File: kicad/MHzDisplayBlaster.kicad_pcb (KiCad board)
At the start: 2 copper layers, 50 x 39 mm, 10 parts, among them J1 Conn_02x15 DigitLHS, J2 Conn_02x15 DigitRHS, J3 Conn_01x03_Pin, J4 Conn_01x02_Pin, Q1 2N7000, U1 DC56-11GWA, U2 74HC04

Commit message: Add version silkscreen
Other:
- board text added: "V1.1"
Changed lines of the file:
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@@
+		)
+	)
+	(gr_text "V1.1"
+		(at 146.05 41.313236 0)
+		(layer "B.SilkS")
+		(effects
+			(font
+				(size 0.8 0.8)
+				(thickness 0.15)
+			)
+			(justify mirror)
 		)
 	)

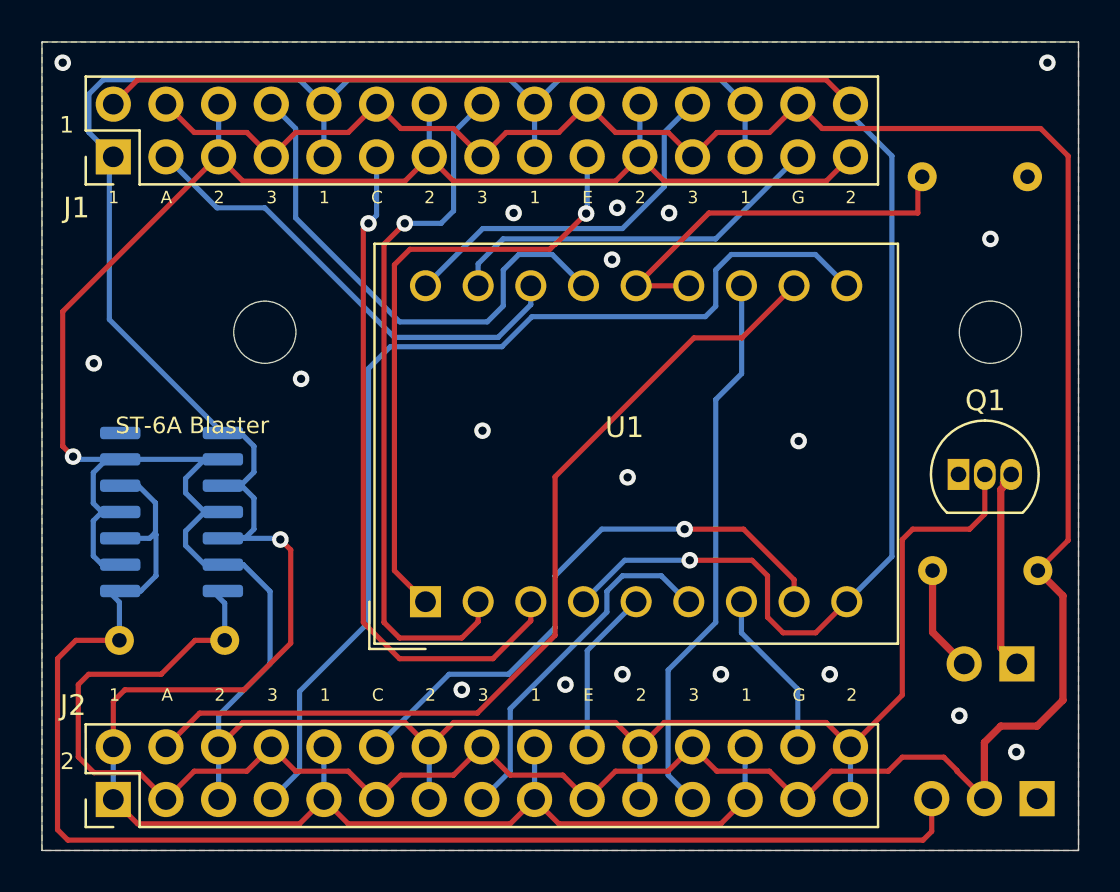
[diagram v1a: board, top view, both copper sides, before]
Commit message: v1.2 - surface mount and better power management
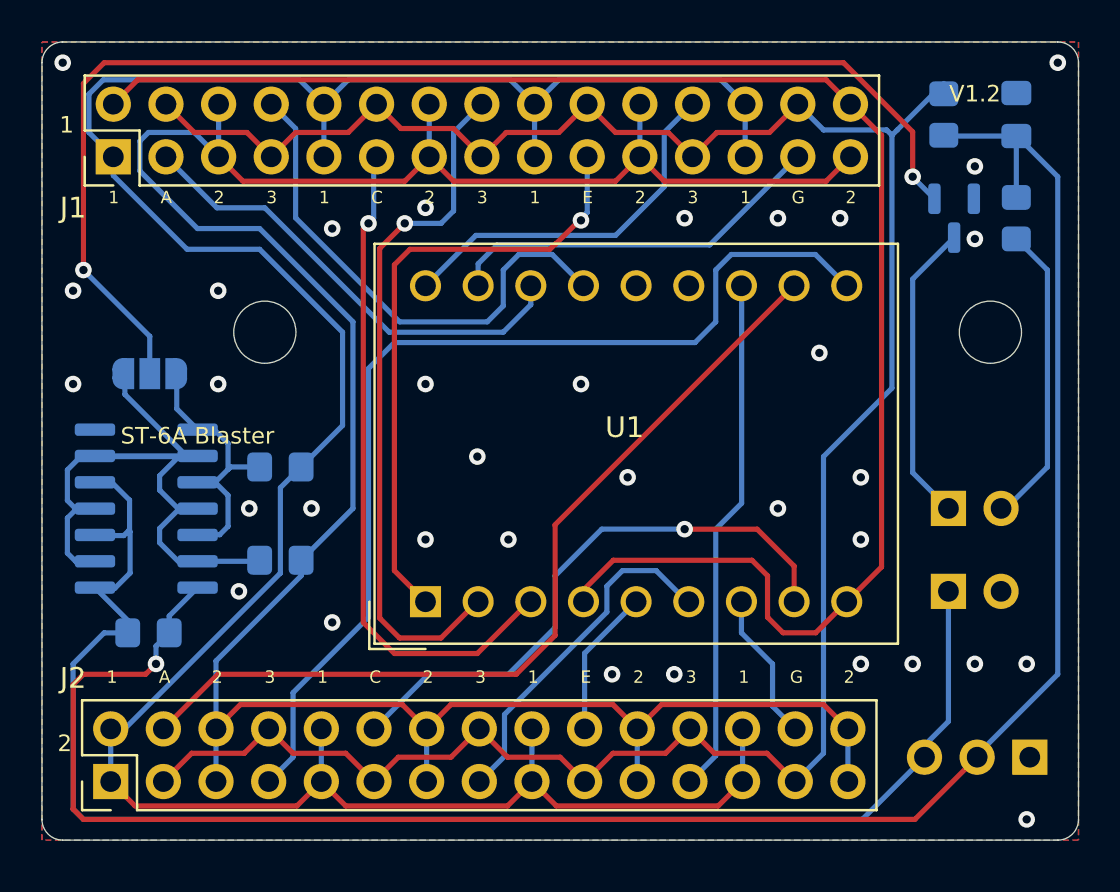
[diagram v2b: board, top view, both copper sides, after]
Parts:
- added C1: 10uf, Capacitor_SMD:C_0805_2012Metric_Pad1.18x1.45mm_HandSolder, B.Cu at (147.0, 43.5)
- added J5: SW, Connector_PinHeader_2.54mm:PinHeader_1x02_P2.54mm_Vertical, B.Cu at (143.7, 66.5)
- added JP1: Jumper_3_Open, Jumper:SolderJumper-3_P1.3mm_Open_RoundedPad1.0x1.5mm, B.Cu at (105.2, 56.0)
- added R4: 330, Resistor_SMD:R_0805_2012Metric_Pad1.20x1.40mm_HandSolder, B.Cu at (111.5, 60.5)
- added R5: 330, Resistor_SMD:R_0805_2012Metric_Pad1.20x1.40mm_HandSolder, B.Cu at (111.5, 65.0)
- J3: value Conn_01x03_Pin -> INPUT
- J4: value Conn_01x02_Pin -> LED
- Q1: value 2N7000 -> 2N7002; footprint Package_TO_SOT_THT:TO-92_Inline -> Package_TO_SOT_SMD:SOT-23; moved to B.Cu
- R1: value 100 -> 330; footprint Resistor_THT:R_Axial_DIN0204_L3.6mm_D1.6mm_P5.08mm_Horizontal -> Resistor_SMD:R_0805_2012Metric_Pad1.20x1.40mm_HandSolder
- R2: value 1K -> 10k; footprint Resistor_THT:R_Axial_DIN0204_L3.6mm_D1.6mm_P5.08mm_Horizontal -> Resistor_SMD:R_0805_2012Metric_Pad1.20x1.40mm_HandSolder
- R3: footprint Resistor_THT:R_Axial_DIN0204_L3.6mm_D1.6mm_P5.08mm_Horizontal -> Resistor_SMD:R_0805_2012Metric_Pad1.20x1.40mm_HandSolder
- U2: value 74HC04 -> 74HCT04
- moved R3 17.5 mm to (147.0, 48.5), turned to 90 degrees
- moved Q1 12.4 mm to (144.0, 48.5), turned to -90 degrees
- moved J4 8.19 mm to (143.7, 62.5), turned to -90 degrees
- moved R1 5.03 mm to (143.5, 43.5), turned to 90 degrees
- moved R2 3.70 mm to (105.1, 68.5)
- moved J3 2.03 mm to (147.7, 74.5)
- moved U2 1.23 mm to (105.0, 62.5)
- moved J2 0.87 mm to (103.3, 75.7)
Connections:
- J3 pad 2: 3 -> +5V
- Q1 pad 1: GND -> LED_SW
- Q1 pad 2: 2 -> GND
- R1 pad 1: GND -> +5V
- R1 pad 2: DIG1_CC -> 3
- R2 pad 1: 3 -> +5V
- R3 pad 2: 3 -> +5V
- U1 pad 13: DIG1_CC -> GND
- U1 pad 14: DIG1_CC -> GND
- U2 pad 10: 1 -> Net-(JP1-A)
- U2 pad 11: 2 -> Net-(JP1-B)
- U2 pad 12: 1 -> Net-(JP1-A)
- U2 pad 13: 2 -> Net-(JP1-B)
- U2 pad 14: 3 -> +5V
- U2 pad 2: 2 -> Net-(JP1-B)
- U2 pad 4: 2 -> Net-(JP1-B)
- U2 pad 6: 2 -> Net-(JP1-B)
- U2 pad 8: 1 -> Net-(JP1-A)
- U2 pad 9: 2 -> Net-(JP1-B)
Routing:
- net +5V: track 0.00 -> 98.8 mm, vias 0 -> 1
- net LED_SW: track 0.00 -> 60.8 mm, vias 0 -> 2
- net 3: track 152.1 -> 115.6 mm
- net Net-(JP1-B): track 0.00 -> 33.0 mm
- net 2: track 152.8 -> 126.2 mm, vias 1 -> 0
- net DIG1_CC: track 19.4 -> 0.00 mm
- net Net-(JP1-A): track 0.00 -> 15.1 mm
- net Net-(J4-Pin_2): track 5.13 -> 14.8 mm
- net 1: track 134.7 -> 128.3 mm, vias 1 -> 0
- net Turbo: track 69.2 -> 74.9 mm
- net Net-(J4-Pin_1): track 9.67 -> 14.9 mm
- net DIG2_F: track 26.7 -> 25.0 mm
- net DIG2_A: track 44.0 -> 42.4 mm
- net DIG2_G: track 8.13 -> 7.21 mm
- net DIG2_E: track 7.98 -> 7.16 mm
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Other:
- board size 50 x 39 mm -> 50 x 38.5 mm
- board text added: "+LED-"
- board text added: "L H"
- board text added: "V1.2"
- board text removed: "-LED+"
- board text removed: "100"
- board text removed: "1k"
- board text removed: "330"
- board text removed: "V1.1"

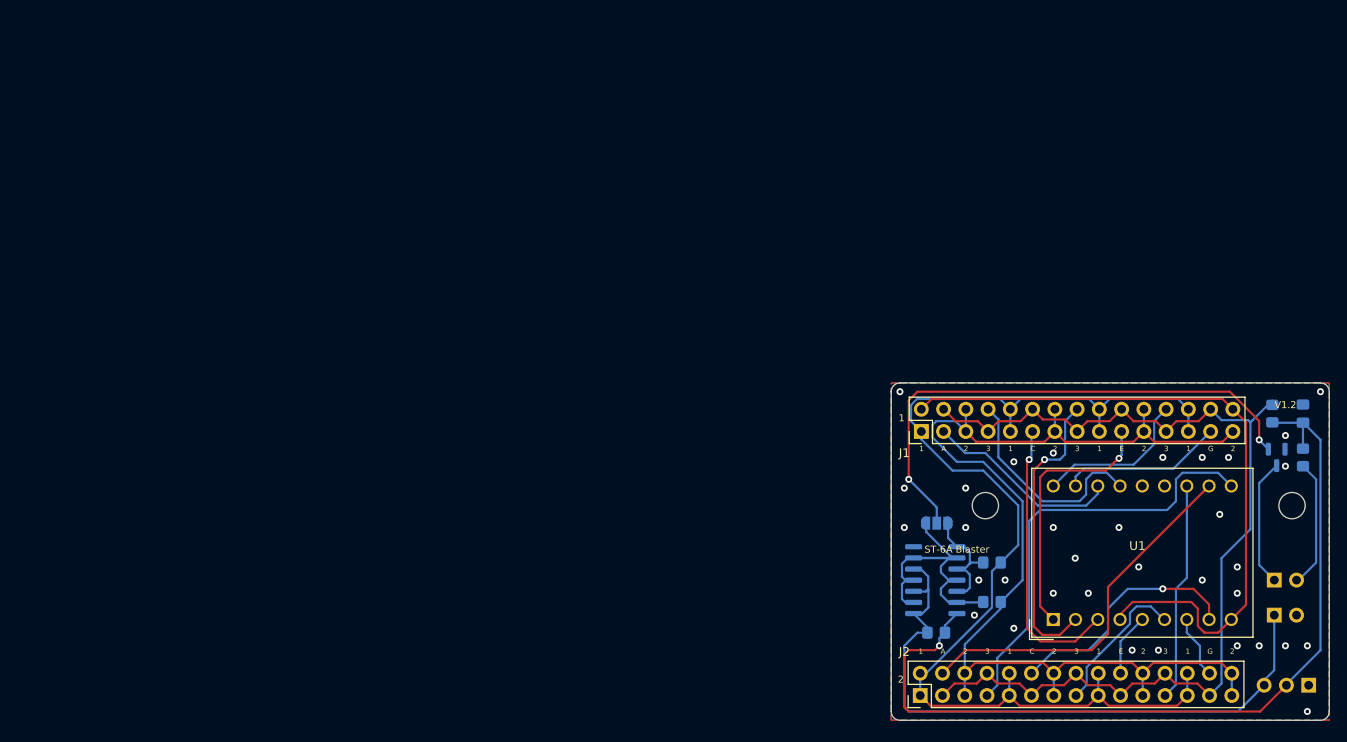
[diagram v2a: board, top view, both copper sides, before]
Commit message: Added Individual segment resistors
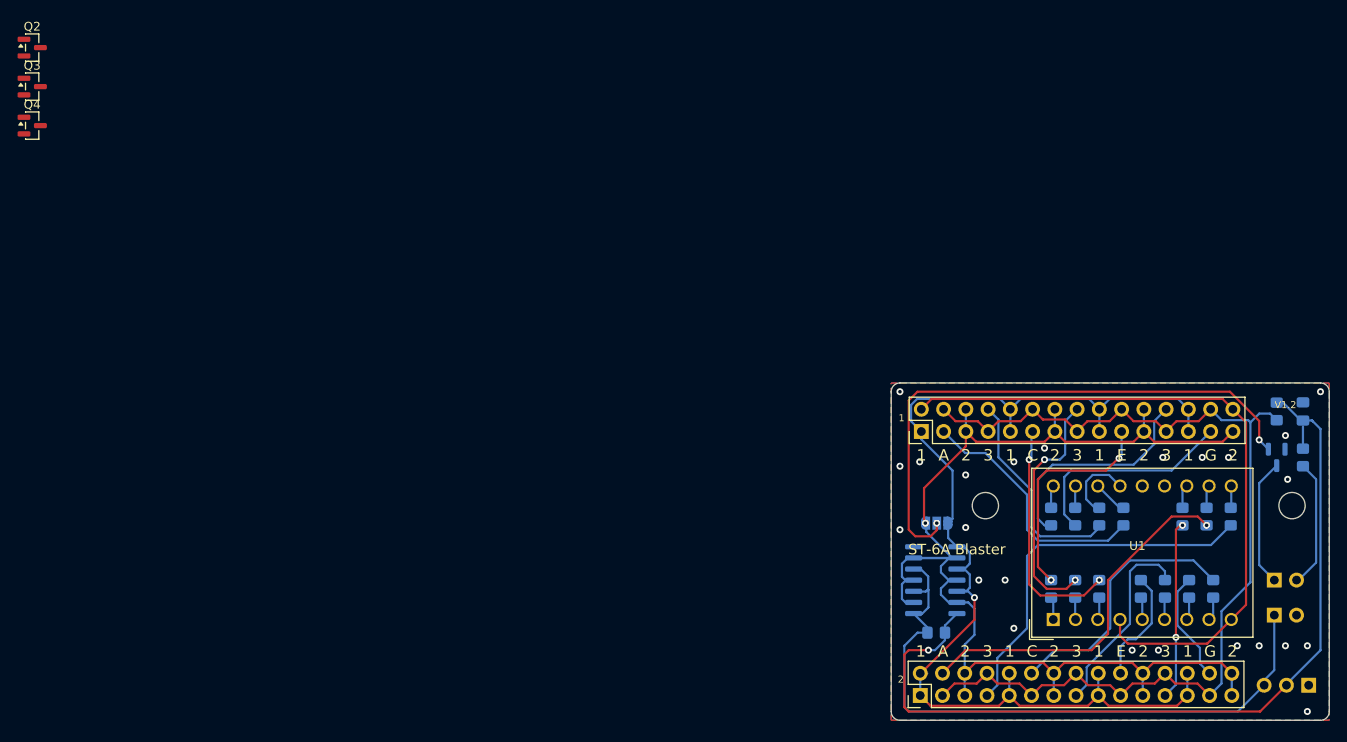
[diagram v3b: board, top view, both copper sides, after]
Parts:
- added Q2: AO3401A, Package_TO_SOT_SMD:SOT-23, F.Cu at (1.96, 1.73)
- added Q3: AO3401A, Package_TO_SOT_SMD:SOT-23, F.Cu at (1.96, 6.17)
- added Q4: AO3401A, Package_TO_SOT_SMD:SOT-23, F.Cu at (1.96, 10.6)
- added R10: 330, Resistor_SMD:R_0805_2012Metric_Pad1.20x1.40mm_HandSolder, B.Cu at (121.0, 55.2)
- added R11: 330, Resistor_SMD:R_0805_2012Metric_Pad1.20x1.40mm_HandSolder, B.Cu at (136.0, 55.2)
- added R12: 330, Resistor_SMD:R_0805_2012Metric_Pad1.20x1.40mm_HandSolder, B.Cu at (138.8, 55.2)
- added R13: 330, Resistor_SMD:R_0805_2012Metric_Pad1.20x1.40mm_HandSolder, B.Cu at (136.8, 63.5)
- added R14: 330, Resistor_SMD:R_0805_2012Metric_Pad1.20x1.40mm_HandSolder, B.Cu at (131.2, 63.5)
- added R15: 330, Resistor_SMD:R_0805_2012Metric_Pad1.20x1.40mm_HandSolder, B.Cu at (128.5, 63.5)
- added R16: 330, Resistor_SMD:R_0805_2012Metric_Pad1.20x1.40mm_HandSolder, B.Cu at (133.2, 55.2)
- added R17: 330, Resistor_SMD:R_0805_2012Metric_Pad1.20x1.40mm_HandSolder, B.Cu at (134.0, 63.5)
- added R6: 330, Resistor_SMD:R_0805_2012Metric_Pad1.20x1.40mm_HandSolder, B.Cu at (123.8, 63.5)
- added R7: 330, Resistor_SMD:R_0805_2012Metric_Pad1.20x1.40mm_HandSolder, B.Cu at (121.0, 63.5)
- added R8: 330, Resistor_SMD:R_0805_2012Metric_Pad1.20x1.40mm_HandSolder, B.Cu at (118.2, 63.5)
- added R9: 330, Resistor_SMD:R_0805_2012Metric_Pad1.20x1.40mm_HandSolder, B.Cu at (118.2, 55.2)
- R1: value 330 -> 100
- moved R4 15.9 mm to (126.5, 55.2), turned to -90 degrees
- moved R5 15.7 mm to (123.8, 55.2), turned to -90 degrees
- moved R1 0.56 mm to (144.0, 43.2), turned to -90 degrees
- moved C1 0.25 mm to (147.0, 43.2)
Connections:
- JP1 pad 1: Net-(JP1-A) -> 1
- JP1 pad 3: Net-(JP1-B) -> 2
- R4 pad 1: 1 -> Net-(U1-DIG1_A)
- R4 pad 2: Net-(JP1-A) -> DIG1_A
- R5 pad 1: 2 -> Net-(U1-DIG1_B)
- R5 pad 2: Net-(JP1-B) -> DIG1_B
- U1 pad 1: DIG1_E -> Net-(U1-DIG1_E)
- U1 pad 10: DIG2_B -> Net-(U1-DIG2_B)
- U1 pad 11: DIG2_A -> Net-(U1-DIG2_A)
- U1 pad 12: DIG2_F -> Net-(U1-DIG2_F)
- U1 pad 15: DIG1_B -> Net-(U1-DIG1_B)
- U1 pad 16: DIG1_A -> Net-(U1-DIG1_A)
- U1 pad 17: DIG1_G -> Net-(U1-DIG1_G)
- U1 pad 18: DIG1_F -> Net-(U1-DIG1_F)
- U1 pad 2: DIG1_D -> Net-(U1-DIG1_D)
- U1 pad 3: DIG1_C -> Net-(U1-DIG1_C)
- U1 pad 5: DIG2_E -> Net-(U1-DIG2_E)
- U1 pad 6: DIG2_D -> Net-(U1-DIG2_D)
- U1 pad 7: DIG2_G -> Net-(U1-DIG2_G)
- U1 pad 8: DIG2_C -> Net-(U1-DIG2_C)
- U2 pad 10: Net-(JP1-A) -> 1
- U2 pad 11: Net-(JP1-B) -> 2
- U2 pad 12: Net-(JP1-A) -> 1
- U2 pad 13: Net-(JP1-B) -> 2
- U2 pad 2: Net-(JP1-B) -> 2
- U2 pad 4: Net-(JP1-B) -> 2
- U2 pad 6: Net-(JP1-B) -> 2
- U2 pad 8: Net-(JP1-A) -> 1
- U2 pad 9: Net-(JP1-B) -> 2
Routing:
- net Net-(JP1-B): track 33.0 -> 0.00 mm
- net Net-(JP1-A): track 15.1 -> 0.00 mm
- net 2: track 126.2 -> 137.3 mm, vias 0 -> 1
- net Net-(U1-DIG1_B): track 0.00 -> 8.38 mm
- net DIG1_F: track 18.0 -> 25.8 mm
- net DIG2_B: track 49.4 -> 42.5 mm
- net DIG1_G: track 18.6 -> 24.9 mm
- net DIG1_A: track 22.6 -> 28.6 mm
- net DIG2_E: track 7.16 -> 13.2 mm
- net DIG1_D: track 33.7 -> 27.8 mm, vias 1 -> 2
- net DIG1_C: track 32.5 -> 26.9 mm, vias 1 -> 2
- net DIG2_G: track 7.21 -> 12.7 mm
- net DIG2_D: track 16.9 -> 22.3 mm
- net DIG2_F: track 25.0 -> 20.4 mm, vias 0 -> 2
- net DIG1_E: track 29.9 -> 25.6 mm, vias 1 -> 2
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
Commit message: v1.3 - Anode resistors, mosfet power delivery, single channel inverter
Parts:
- removed the R1 at (144.0, 43.2)
- added R18: 470, Resistor_SMD:R_0805_2012Metric_Pad1.20x1.40mm_HandSolder, B.Cu at (109.2, 67.2)
- added R19: 470, Resistor_SMD:R_0805_2012Metric_Pad1.20x1.40mm_HandSolder, B.Cu at (109.2, 60.8)
- added R2: 470, Resistor_SMD:R_0805_2012Metric_Pad1.20x1.40mm_HandSolder, B.Cu at (102.5, 60.8)
- C1: value 10uf -> 0.1uF
- Q2, Q3, Q4: value AO3401A -> Si2301; footprint Package_TO_SOT_SMD:SOT-23 -> Package_TO_SOT_SMD:SOT-23-3; moved to B.Cu
- U2: value 74HCT04 -> 74LVC1G04; footprint Package_SO:SOIC-14_3.9x8.7mm_P1.27mm -> Package_TO_SOT_SMD:SOT-353_SC-70-5
- moved Q2 128.3 mm to (112.2, 67.2), turned to 180 degrees
- moved Q3 123.1 mm to (112.2, 60.8), turned to 180 degrees
- moved Q4 111.0 mm to (103.7, 54.9), turned to -90 degrees
- moved C1 48.3 mm to (103.5, 64.2), turned to 0 degrees
- moved U2 4.99 mm to (105.2, 67.5), turned to 180 degrees
- moved JP1 4.80 mm to (105.2, 60.8), turned to -90 degrees
- moved R1 2.82 mm to (102.5, 67.5), turned to -90 degrees
- moved Q1 2.07 mm to (144.2, 46.4)
- moved R3 2.07 mm to (147.2, 46.4)
- renumbered R2 to R1
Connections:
- JP1 pad 1: 1 -> Net-(JP1-A)
- JP1 pad 3: 2 -> Net-(JP1-B)
- Q1 pad 1: LED_SW -> Net-(Q1-G)
- Q2 pad 1: unconnected-(Q2-G-Pad1) -> Net-(JP1-B)
- Q2 pad 2: unconnected-(Q2-S-Pad2) -> 2
- Q2 pad 3: unconnected-(Q2-D-Pad3) -> +5V
- Q3 pad 1: unconnected-(Q3-G-Pad1) -> Net-(JP1-A)
- Q3 pad 2: unconnected-(Q3-S-Pad2) -> 1
- Q3 pad 3: unconnected-(Q3-D-Pad3) -> +5V
- Q4 pad 1: unconnected-(Q4-G-Pad1) -> GND
- Q4 pad 2: unconnected-(Q4-S-Pad2) -> 3
- Q4 pad 3: unconnected-(Q4-D-Pad3) -> +5V
- U2 pad 1: Turbo -> unconnected-(U2-NC-Pad1)
- U2 pad 2: 2 -> Turbo
- U2 pad 3: Turbo -> GND
- U2 pad 4: 2 -> Net-(R19-Pad1)
- U2 pad 5: Turbo -> +5V
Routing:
- net Net-(Q1-G): track 0.00 -> 63.6 mm, vias 0 -> 2
- net LED_SW: track 64.8 -> 3.16 mm
- net Net-(JP1-B): track 0.00 -> 28.1 mm
- net +5V: track 99.7 -> 121.3 mm, vias 1 -> 4
- net 2: track 137.3 -> 117.7 mm
- net Net-(R19-Pad1): track 0.00 -> 8.50 mm, vias 0 -> 2
- net GND: track 0.00 -> 8.35 mm, vias 24 -> 2
- net Net-(JP1-A): track 0.00 -> 8.26 mm
- net 3: track 115.8 -> 123.1 mm, vias 0 -> 1
- net Turbo: track 74.9 -> 68.4 mm
- net DP: track 78.5 -> 81.9 mm
- net Net-(J4-Pin_2): track 14.8 -> 16.3 mm, vias 0 -> 1
- net Net-(J4-Pin_1): track 14.9 -> 16.2 mm, vias 0 -> 1
- net 1: track 128.1 -> 128.9 mm
- removed copper zone on F.Cu, net GND
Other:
- board text added: "(R4 - R17)"
- board text added: "LED"
- board text added: "V1.3"
- board text removed: "L H"
- board text removed: "V1.2"

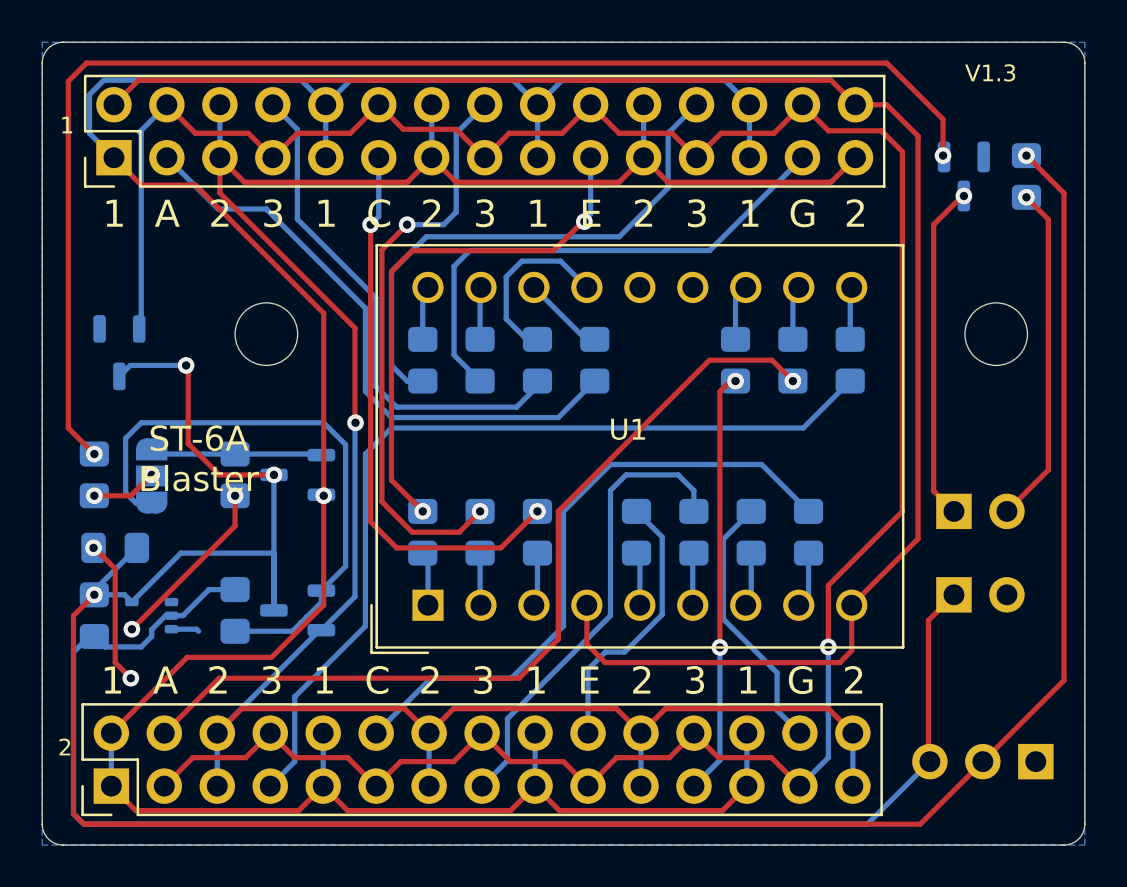
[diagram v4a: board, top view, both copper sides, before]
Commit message: v1.4 - Swap Si2301 pins for proper source and drain, fix 2N7002 gate
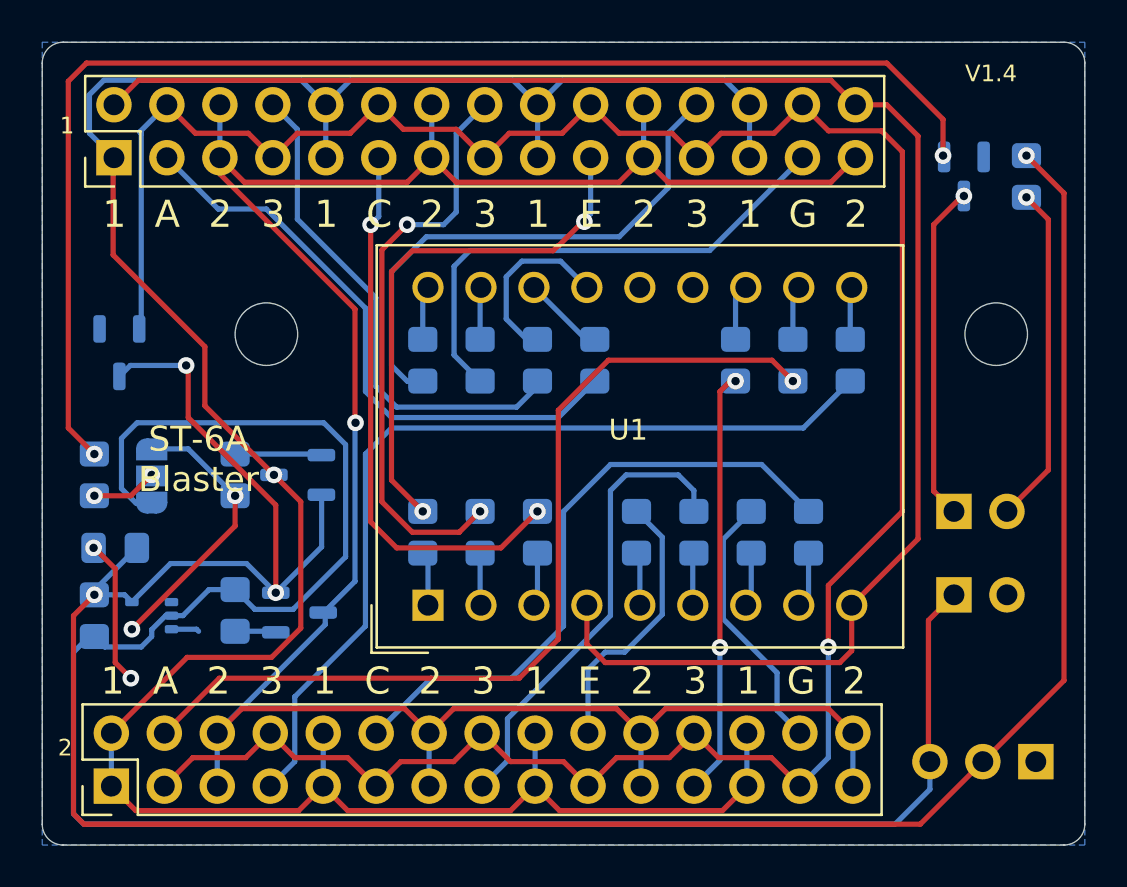
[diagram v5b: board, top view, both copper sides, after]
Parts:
- moved Q2 0.13 mm to (112.3, 67.3), turned to 0 degrees
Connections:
- JP1 pad 3: Net-(JP1-B) -> Turbo
- Q2 pad 1: Net-(JP1-B) -> Net-(Q2-G)
- Q2 pad 2: 2 -> +5V
- Q2 pad 3: +5V -> 2
- Q3 pad 1: Net-(JP1-A) -> Net-(Q3-G)
- Q3 pad 2: 1 -> +5V
- Q3 pad 3: +5V -> 1
- R18 pad 2: Net-(JP1-B) -> Net-(Q2-G)
- R19 pad 1: Net-(R19-Pad1) -> Net-(JP1-A)
- R19 pad 2: Net-(JP1-A) -> Net-(Q3-G)
- U2 pad 4: Net-(R19-Pad1) -> Net-(JP1-A)
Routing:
- net Turbo: track 68.4 -> 96.9 mm
- net Net-(JP1-B): track 28.1 -> 0.00 mm
- net Net-(R19-Pad1): track 8.50 -> 0.00 mm, vias 2 -> 0
- net Net-(JP1-A): track 8.26 -> 13.8 mm, vias 0 -> 2
- net Net-(Q3-G): track 0.00 -> 4.16 mm
- net DIG2_A: track 41.6 -> 44.4 mm
- net 1: track 128.9 -> 126.5 mm
- net Net-(Q2-G): track 0.00 -> 1.97 mm
- net +5V: track 121.3 -> 122.5 mm
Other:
- board text added: "V1.4"
- board text removed: "V1.3"
